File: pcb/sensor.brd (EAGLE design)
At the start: 68.6 x 53.3 mm, 14 parts, among them IC2 4512N, Q1 BUZ10, U1 ARDUINOR3-DIMENSION

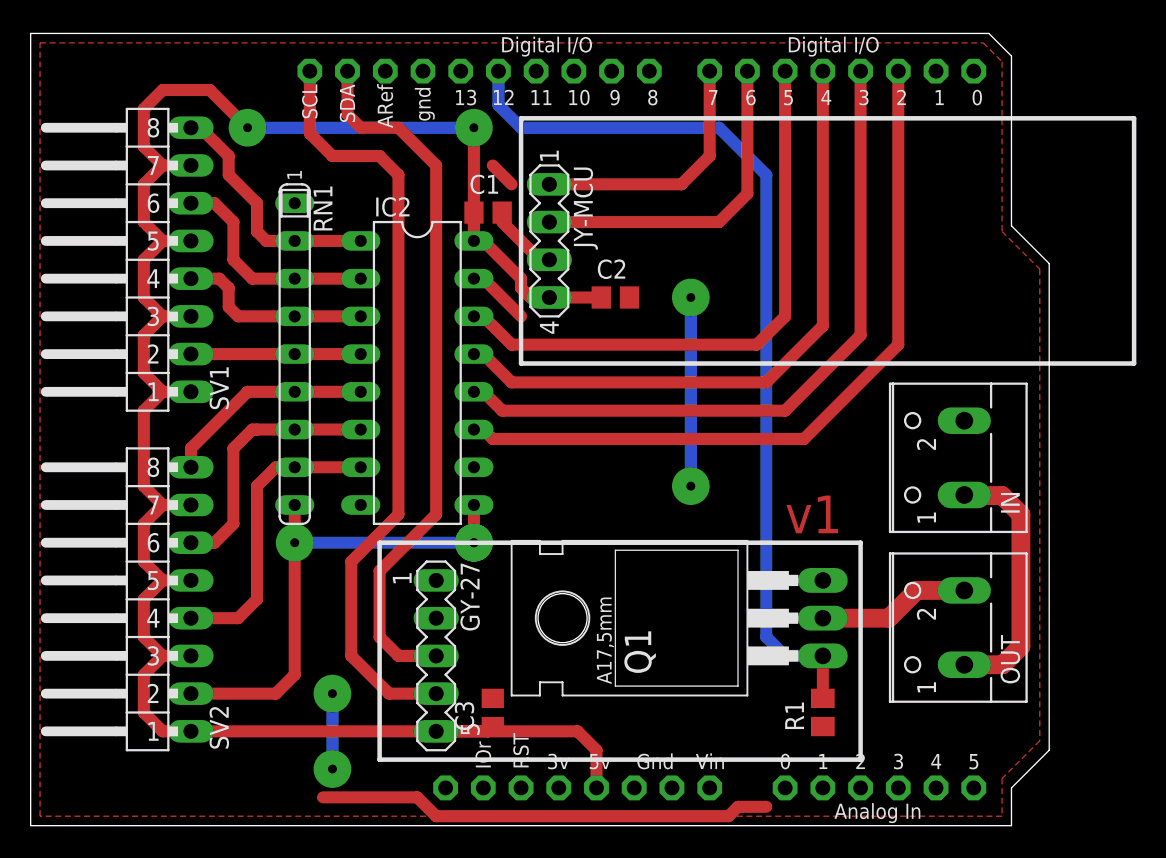
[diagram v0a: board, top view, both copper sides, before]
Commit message: Added led strip connector
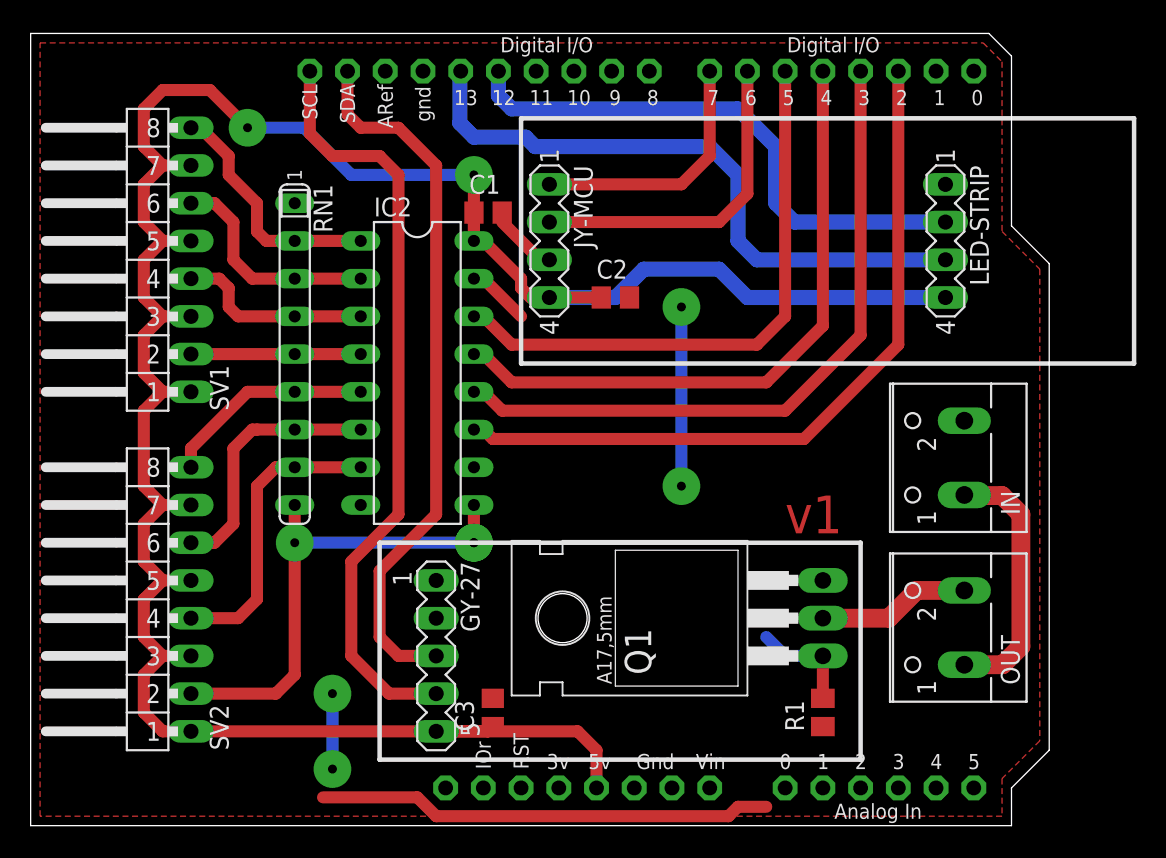
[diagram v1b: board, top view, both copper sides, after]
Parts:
- added LED-STRIP: (no value), con-lstb:MA04-1
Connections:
- removed net N$8: U1.D13
- new net CO: LED-STRIP.2, U1.D12
- new net DO: LED-STRIP.3, U1.D13
- net +5V: now also LED-STRIP.4
- net POUT: now also U1.A5; no longer U1.D12
- net VSS: now also LED-STRIP.1
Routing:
- net POUT: track 60.6 -> 7.20 mm
- net DO: track 0.00 -> 42.6 mm
- net CO: track 0.00 -> 37.5 mm
- net +5V: track 143.2 -> 169.6 mm
- net VSS: track 58.7 -> 56.2 mm
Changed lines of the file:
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@@
 <element name="IC2" library="45xx" package="DIL16" value="4512N" x="26.035" y="30.48" rot="R270"/>
 <element name="Q1" library="transistor-fet" package="TO220" value="BUZ10" x="46.99" y="13.97" rot="R90"/>
+<element name="LED-STRIP" library="con-lstb" package="MA04-1" value="" x="61.595" y="39.37" rot="R270">
+<attribute name="OC_NEWARK" value="unknown" x="61.595" y="39.37" size="2.54" layer="27" rot="R270" display="off"/>
+<attribute name="MPN" value="" x="61.595" y="39.37" size="2.54" layer="27" rot="R270" display="off"/>
+<attribute name="MF" value="" x="61.595" y="39.37" size="2.54" layer="27" rot="R270" display="off"/>
+<attribute name="OC_FARNELL" value="unknown" x="61.595" y="39.37" size="2.54" layer="27" rot="R270" display="off"/>
+</element>
 </elements>
 <signals>
@@
 <contactref element="IC2" pad="15"/>
 <contactref element="IC2" pad="8"/>
-<wire x1="32.385" y1="43.18" x2="31.115" y2="44.45" width="0.8128" layer="1"/>
 <contactref element="Q1" pad="3"/>
 <wire x1="19.685" y1="1.905" x2="26.035" y2="1.905" width="0.8128" layer="1"/>
@@
 <wire x1="46.99" y1="0.635" x2="47.625" y2="1.27" width="0.8128" layer="1"/>
 <wire x1="47.625" y1="1.27" x2="49.53" y2="1.27" width="0.8128" layer="1"/>
-<via x="44.45" y="35.56" extent="1-16" drill="0.6" diameter="2.54"/>
-<via x="44.45" y="22.86" extent="1-16" drill="0.6" diameter="2.54"/>
-<wire x1="44.45" y1="35.56" x2="44.45" y2="22.86" width="0.8128" layer="16"/>
+<via x="43.815" y="34.925" extent="1-16" drill="0.6" diameter="2.54"/>
+<via x="43.815" y="22.86" extent="1-16" drill="0.6" diameter="2.54"/>
+<wire x1="43.815" y1="34.925" x2="43.815" y2="22.86" width="0.8128" layer="16"/>
 <via x="20.32" y="8.89" extent="1-16" drill="0.6" diameter="2.54"/>
 <via x="20.32" y="3.81" extent="1-16" drill="0.6" diameter="2.54"/>
@@
 <wire x1="34.925" y1="38.1" x2="34.29" y2="38.1" width="0.8128" layer="1"/>
 <wire x1="34.29" y1="38.1" x2="31.75" y2="40.64" width="0.8128" layer="1"/>
+<contactref element="LED-STRIP" pad="1"/>
 </signal>
 <signal name="VIN">
@@
 <wire x1="12.065" y1="49.53" x2="14.605" y2="46.99" width="0.8128" layer="1"/>
 <via x="14.605" y="46.99" extent="1-16" drill="0.6" diameter="2.54"/>
-<via x="29.845" y="46.99" extent="1-16" drill="0.6" diameter="2.54"/>
-<wire x1="14.605" y1="46.99" x2="29.845" y2="46.99" width="0.8128" layer="16"/>
-<wire x1="29.845" y1="46.99" x2="29.845" y2="39.37" width="0.8128" layer="1"/>
+<via x="29.845" y="43.815" extent="1-16" drill="0.6" diameter="2.54"/>
+<wire x1="14.605" y1="46.99" x2="18.415" y2="46.99" width="0.8128" layer="16"/>
+<wire x1="18.415" y1="46.99" x2="21.59" y2="43.815" width="0.8128" layer="16"/>
+<wire x1="21.59" y1="43.815" x2="29.845" y2="43.815" width="0.8128" layer="16"/>
+<wire x1="29.845" y1="43.815" x2="29.845" y2="39.37" width="0.8128" layer="1"/>
 <wire x1="29.8475" y1="41.275" x2="29.8475" y2="39.3725" width="0.8128" layer="1"/>
 <wire x1="29.8475" y1="39.3725" x2="29.845" y2="39.37" width="0.8128" layer="1"/>
+<contactref element="LED-STRIP" pad="4"/>
+<wire x1="61.595" y1="35.56" x2="48.26" y2="35.56" width="1.016" layer="16"/>
+<wire x1="48.26" y1="35.56" x2="46.355" y2="37.465" width="1.016" layer="16"/>
+<wire x1="46.355" y1="37.465" x2="41.275" y2="37.465" width="1.016" layer="16"/>
+<wire x1="41.275" y1="37.465" x2="39.37" y2="35.56" width="1.016" layer="16"/>
+<wire x1="39.37" y1="35.56" x2="34.925" y2="35.56" width="1.016" layer="16"/>
 </signal>
 <signal name="N$4">
@@
 <wire x1="50.8" y1="34.29" x2="50.8" y2="50.8" width="0.8128" layer="1"/>
 </signal>
-<signal name="N$8">
-<contactref element="U1" pad="D13"/>
-</signal>
 <signal name="SDA">
 <contactref element="U1" pad="SDA"/>
@@
 <signal name="POUT">
 <contactref element="R1" pad="2"/>
-<contactref element="U1" pad="D12"/>
 <contactref element="Q1" pad="1"/>
 <wire x1="53.34" y1="11.43" x2="53.34" y2="8.57" width="0.8128" layer="1"/>
-<wire x1="31.496" y1="50.8" x2="31.496" y2="48.514" width="0.8128" layer="16"/>
-<wire x1="31.496" y1="48.514" x2="33.02" y2="46.99" width="0.8128" layer="16"/>
-<wire x1="33.02" y1="46.99" x2="46.355" y2="46.99" width="0.8128" layer="16"/>
-<wire x1="46.355" y1="46.99" x2="49.53" y2="43.815" width="0.8128" layer="16"/>
-<wire x1="49.53" y1="43.815" x2="49.53" y2="12.7" width="0.8128" layer="16"/>
 <wire x1="49.53" y1="12.7" x2="50.8" y2="11.43" width="0.8128" layer="16"/>
 <wire x1="50.8" y1="11.43" x2="53.34" y2="11.43" width="0.8128" layer="16"/>
+<contactref element="U1" pad="A5"/>
+<wire x1="53.34" y1="8.57" x2="63.5" y2="2.54" width="0" layer="19" extent="1-1"/>
 </signal>
 <signal name="+15V">
@@
 <via x="29.845" y="19.05" extent="1-16" drill="0.6" diameter="2.54"/>
 </signal>
+<signal name="CO">
+<contactref element="LED-STRIP" pad="2"/>
+<contactref element="U1" pad="D12"/>
+<wire x1="61.595" y1="40.64" x2="51.435" y2="40.64" width="1.016" layer="16"/>
+<wire x1="51.435" y1="40.64" x2="50.165" y2="41.91" width="1.016" layer="16"/>
+<wire x1="50.165" y1="41.91" x2="50.165" y2="45.72" width="1.016" layer="16"/>
+<wire x1="50.165" y1="45.72" x2="47.625" y2="48.26" width="1.016" layer="16"/>
+<wire x1="47.625" y1="48.26" x2="32.385" y2="48.26" width="1.016" layer="16"/>
+<wire x1="32.385" y1="48.26" x2="31.496" y2="49.149" width="1.016" layer="16"/>
+<wire x1="31.496" y1="49.149" x2="31.496" y2="50.8" width="1.016" layer="16"/>
+</signal>
+<signal name="DO">
+<contactref element="LED-STRIP" pad="3"/>
+<contactref element="U1" pad="D13"/>
+<wire x1="28.956" y1="50.8" x2="28.8925" y2="50.7365" width="1.016" layer="16"/>
+<wire x1="28.8925" y1="50.7365" x2="28.8925" y2="47.3075" width="1.016" layer="16"/>
+<wire x1="28.8925" y1="47.3075" x2="29.845" y2="46.355" width="1.016" layer="16"/>
+<wire x1="29.845" y1="46.355" x2="33.3375" y2="46.355" width="1.016" layer="16"/>
+<wire x1="33.3375" y1="46.355" x2="33.9725" y2="45.72" width="1.016" layer="16"/>
+<wire x1="33.9725" y1="45.72" x2="45.72" y2="45.72" width="1.016" layer="16"/>
+<wire x1="45.72" y1="45.72" x2="47.625" y2="43.815" width="1.016" layer="16"/>
+<wire x1="47.625" y1="43.815" x2="47.625" y2="39.37" width="1.016" layer="16"/>
+<wire x1="47.625" y1="39.37" x2="48.895" y2="38.1" width="1.016" layer="16"/>
+<wire x1="48.895" y1="38.1" x2="61.595" y2="38.1" width="1.016" layer="16"/>
+</signal>
 </signals>

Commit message: Pcb modification
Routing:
- net POUT: track 7.20 -> 17.4 mm
- net VSS: track 56.2 -> 55.6 mm
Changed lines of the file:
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@@
 <wire x1="47.625" y1="1.27" x2="49.53" y2="1.27" width="0.8128" layer="1"/>
 <via x="43.815" y="34.925" extent="1-16" drill="0.6" diameter="2.54"/>
-<via x="43.815" y="22.86" extent="1-16" drill="0.6" diameter="2.54"/>
-<wire x1="43.815" y1="34.925" x2="43.815" y2="22.86" width="0.8128" layer="16"/>
+<via x="43.815" y="23.495" extent="1-16" drill="0.6" diameter="2.54"/>
+<wire x1="43.815" y1="34.925" x2="43.815" y2="23.495" width="0.8128" layer="16"/>
 <via x="20.32" y="8.89" extent="1-16" drill="0.6" diameter="2.54"/>
 <via x="20.32" y="3.81" extent="1-16" drill="0.6" diameter="2.54"/>
@@
 <contactref element="Q1" pad="1"/>
 <wire x1="53.34" y1="11.43" x2="53.34" y2="8.57" width="0.8128" layer="1"/>
-<wire x1="49.53" y1="12.7" x2="50.8" y2="11.43" width="0.8128" layer="16"/>
-<wire x1="50.8" y1="11.43" x2="53.34" y2="11.43" width="0.8128" layer="16"/>
 <contactref element="U1" pad="A5"/>
-<wire x1="53.34" y1="8.57" x2="63.5" y2="2.54" width="0" layer="19" extent="1-1"/>
+<wire x1="53.34" y1="8.57" x2="56.2" y2="8.57" width="0.8128" layer="1"/>
+<wire x1="56.2" y1="8.57" x2="57.785" y2="6.985" width="0.8128" layer="1"/>
+<wire x1="57.785" y1="6.985" x2="62.23" y2="6.985" width="0.8128" layer="1"/>
+<wire x1="62.23" y1="6.985" x2="63.5" y2="5.715" width="0.8128" layer="1"/>
+<wire x1="63.5" y1="5.715" x2="63.5" y2="2.54" width="0.8128" layer="1"/>
 </signal>
 <signal name="+15V">

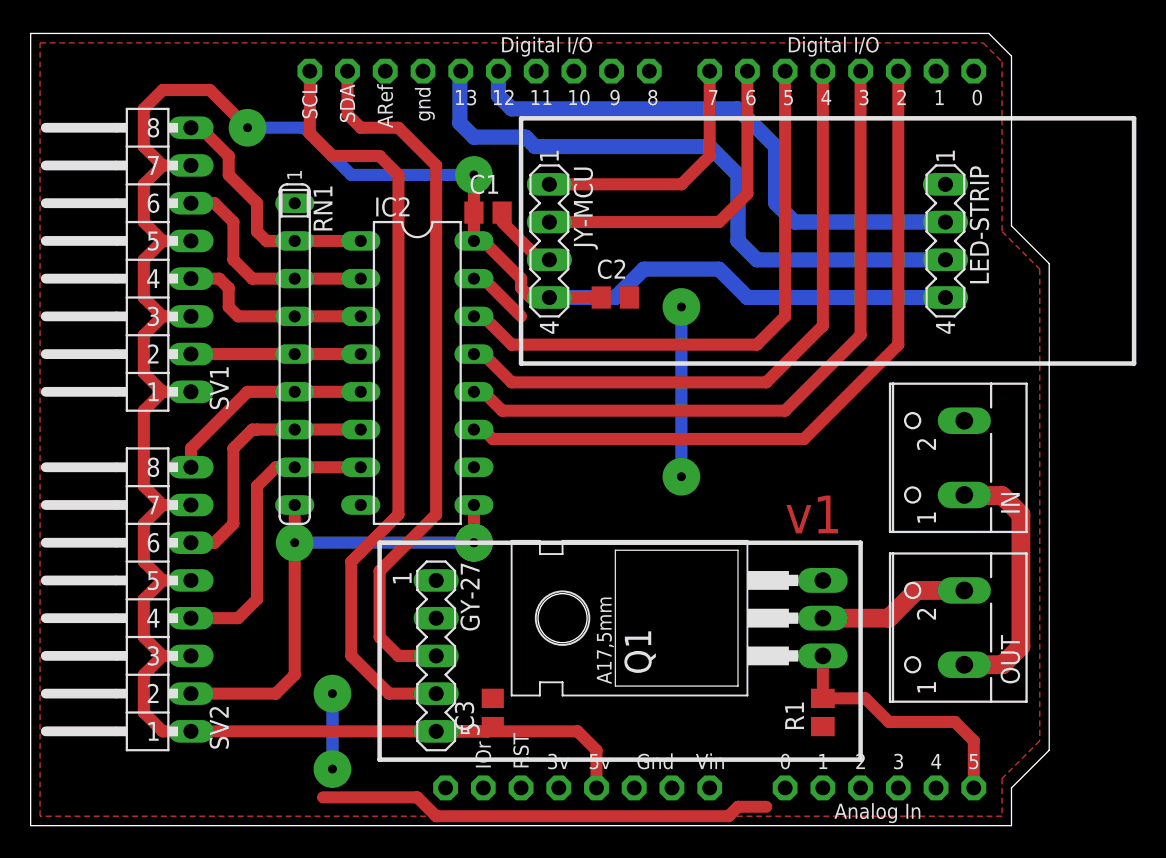
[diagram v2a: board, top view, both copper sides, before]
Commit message: Sensor board milling + Raspberry Pi update
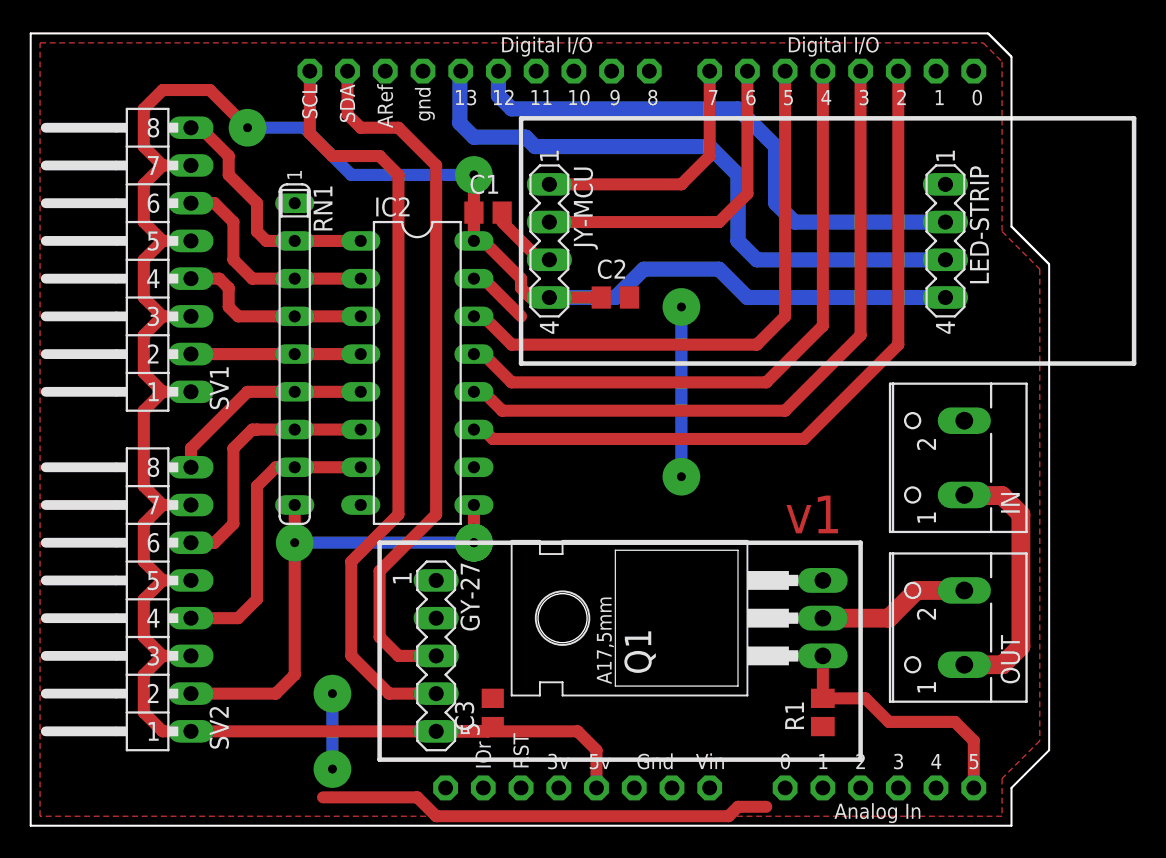
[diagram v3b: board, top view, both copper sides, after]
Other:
- outline, holes or cut-outs redrawn
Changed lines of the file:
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@@
 <setting verticaltext="up"/>
 </settings>
-<grid distance="25" unitdist="mil" unit="mil" style="dots" multiple="1" display="yes" altdistance="0.025" altunitdist="inch" altunit="inch"/>
+<grid distance="12.5" unitdist="mil" unit="mil" style="dots" multiple="1" display="yes" altdistance="0.025" altunitdist="inch" altunit="inch"/>
 <layers>
 <layer number="1" name="Top" color="4" fill="1" visible="yes" active="yes"/>
@@
 <layer number="44" name="Drills" color="7" fill="1" visible="no" active="yes"/>
 <layer number="45" name="Holes" color="7" fill="1" visible="no" active="yes"/>
-<layer number="46" name="Milling" color="3" fill="1" visible="no" active="yes"/>
+<layer number="46" name="Milling" color="3" fill="1" visible="yes" active="yes"/>
 <layer number="47" name="Measures" color="7" fill="1" visible="no" active="yes"/>
 <layer number="48" name="Document" color="7" fill="1" visible="yes" active="yes"/>
@@
 <wire x1="74.295" y1="47.625" x2="33.02" y2="47.625" width="0.3048" layer="21"/>
 <text x="50.8" y="19.685" size="2.54" layer="1">v1</text>
+<wire x1="0" y1="0" x2="0" y2="53.34" width="0.127" layer="46"/>
+<wire x1="0" y1="53.34" x2="64.4525" y2="53.34" width="0.127" layer="46"/>
+<wire x1="64.4525" y1="53.34" x2="66.04" y2="51.7525" width="0.127" layer="46"/>
+<wire x1="66.04" y1="51.7525" x2="66.04" y2="40.3225" width="0.127" layer="46"/>
+<wire x1="66.04" y1="40.3225" x2="68.58" y2="37.7825" width="0.127" layer="46"/>
+<wire x1="68.58" y1="37.7825" x2="68.58" y2="5.08" width="0.127" layer="46"/>
+<wire x1="68.58" y1="5.08" x2="66.04" y2="2.54" width="0.127" layer="46"/>
+<wire x1="66.04" y1="2.54" x2="66.04" y2="0" width="0.127" layer="46"/>
+<wire x1="66.04" y1="0" x2="0" y2="0" width="0.127" layer="46"/>
 </plain>
 <attributes>
